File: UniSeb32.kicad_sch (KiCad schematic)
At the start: 35 parts

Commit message: -
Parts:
- removed X7: (no value), symbol UniSeb8266-eagle-import:0446200002
- added C?: 100n, symbol Device:C_Small
- added J2: ARJM11C7-114-BA-EW2, Connector_RJ:RJ45_Abracon_ARJM11C-BA, symbol Connector-custom:RJ45_Abracon_ARJM11C7-114
- added R? (x2): 2.2k, Resistor_SMD:R_0603_1608Metric, symbol Device:R
- added R? (x4): 49.9 %1, Resistor_SMD:R_0603_1608Metric, symbol Device:R
- added R?: 0, Resistor_SMD:R_0603_1608Metric, symbol Device:R
- C1: value (none) -> 100µF; footprint (none) -> UniSeb8266:E2,5-6
- C2: value (none) -> 22µF; footprint (none) -> UniSeb8266:E2,5-6
- F1: value (none) -> 200mA MT; footprint (none) -> UniSeb8266:TR5
- F2: value (none) -> 1A T; footprint (none) -> UniSeb8266:TR5
- I2C-1, I2C-2, I2C-3: value (none) -> MA05-1_WON; footprint (none) -> UniSeb8266:MA05-1_WON
- IC1: value (none) -> WEMOS-D1-MINI; footprint (none) -> UniSeb8266:WEMOS-D1-MINI
- IC2: value (none) -> GY-BME280-3.3; footprint (none) -> UniSeb8266:GY-BME280-3.3
- IC3: value (none) -> AMS1117-3.3; footprint (none) -> UniSeb8266:SOT223
- IC4: value (none) -> MCP23008SS; footprint (none) -> UniSeb8266:SSOP20
- IC5: value (none) -> RT9400; footprint (none) -> UniSeb8266:RT9400
- IC6: value (none) -> AMS5915; footprint (none) -> UniSeb8266:AMS5915
- J1: value (none) -> 22-?-0327-2031; footprint (none) -> UniSeb8266:6410-03
- LED1: value (none) -> LED3MM; footprint (none) -> UniSeb8266:LED3MM
- R1: value (none) -> 33/1W; footprint (none) -> UniSeb8266:P0613V
- R2: renamed from R?; footprint (none) -> Resistor_SMD:R_0603_1608Metric
- R3: value (none) -> 390; footprint (none) -> UniSeb8266:R1206
- R4: value (none) -> 10k; footprint (none) -> UniSeb8266:R1206
- R5: value (none) -> 4,7k; footprint (none) -> UniSeb8266:R1206
- R6, R7: value (none) -> R-EU_R1206; footprint (none) -> UniSeb8266:R1206
- SJ1: value (none) -> SJ; footprint (none) -> UniSeb8266:SJ
- SJ2: value (none) -> SJ2W; footprint (none) -> UniSeb8266:SJ_2
- U$2: value (none) -> HLK-PM01; footprint (none) -> UniSeb8266:HLK-PM01
- X1, X2: value (none) -> AK500/2; footprint (none) -> UniSeb8266:AK500_2
- X3: value (none) -> 233-503; footprint (none) -> UniSeb8266:233-503
- X5: value (none) -> 233-504; footprint (none) -> UniSeb8266:233-504
- X61: value (none) -> JST-XH-05-PIN-LONG-PAD; footprint (none) -> UniSeb8266:JST-XH-05-PACKAGE-LONG-PAD
- X8: value (none) -> 233-508; footprint (none) -> UniSeb8266:233-508
- gave numbers to parts that had none: 3
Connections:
- net 3V3: now also J2.11 (RLED+), R?.1, R?.1, R?.1, R?.1, R?.2
- net GND: now also C?.1, R?.2, R?.2
- net at U2.20 (TXN): now also J2.8 (TD-), R?.2
- net at U2.21 (TXP): now also J2.10 (TD+), R?.2
- net at U2.22 (RXN): now also J2.3 (RD-), R?.2
- net at U2.23 (RXP): now also J2.5 (RD+), R?.2
- net at U2.3 (LED1/REGOFF): now also J2.13 (LLED+)
- net VA2: now reaches IC5.P$2 (VA2)
- net VA2: now also J2.2 (VC1-)
- net VA1: now reaches IC5.P$1 (VA1)
- net VA1: now also J2.7 (VC1+)
- net VB1: now reaches IC5.P$3 (VB1)
- net VB1: now also J2.6 (VC2+)
- net VB2: now reaches IC5.P$4 (VB2)
- net VB2: now also J2.1 (VC2-)
- new net: J2.12 (RLED-), R?.1
- new net: J2.14 (LLED-), R?.1
- new net: C?.2, J2.4 (RCT), J2.9 (TCT), R?.1
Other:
- moved on the sheet: C3, R2, U1, U2

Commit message: .
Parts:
- added C? (x2): 100n, symbol Device:C_Small
- added C? (x4): 10p, symbol Device:C_Small
- added C?: 10uf, symbol Device:C_Small
- added C?: 22µ, symbol Device:C_Small
- added C?: 2.2µ, symbol Device:C_Small
- added C?: 10n, symbol Device:C_Small
- added L?: L, Inductor_SMD:L_0805_2012Metric, symbol Device:L
- added R?: 12.1k, Resistor_SMD:R_0603_1608Metric, symbol Device:R
- C?: jlcpcb (none) -> C14663
- R? (x2): jlcpcb (none) -> C22938
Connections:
- net 3V3: now also U2.9 (VDDIO), C?.1, C?.1, L?.1; no longer R?.1, R?.1, R?.1, R?.1, R?.2
- net GND: now also U2.25 (VSS), C?.2, C?.2, C?.2, C?.2, C?.2, C?.2, C?.2, C?.2, C?.2, C?.2, R?.2
- net 3V3-2: now reaches U2.1 (VDD2A)
- net 3V3-2: now also R?.1, R?.1, R?.1, R?.1, R?.2, U2.19 (VDD1A), C?.1, C?.1, L?.2
- net at J2.8 (TD-), R?.2, U2.20 (TXN): now also C?.1
- net at J2.10 (TD+), R?.2, U2.21 (TXP): now also C?.1
- net at J2.3 (RD-), R?.2, U2.22 (RXN): now also C?.1
- net at J2.5 (RD+), R?.2, U2.23 (RXP): now also C?.1
- net at U2.24 (RBIAS): now also R?.1
- net at U2.6 (VDDCR): now also C?.1, C?.1

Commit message: .
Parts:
- added C? (x2): 30p, symbol Device:C_Small
- added R? (x6): 10k, Resistor_SMD:R_0603_1608Metric, symbol Device:R
- added Y?: Crystal_GND23, Crystal:Crystal_SMD_3225-4Pin_3.2x2.5mm, symbol Device:Crystal_GND23
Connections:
- net 3V3-2: now also R?.2, R?.2, R?.2, R?.2, R?.2
- net GND: now also C?.2, C?.2, R?.1, Y?.2, Y?.3
- net at U2.10 (RXER/PHYAD0): now also R?.2
- net EMAC_CRS_DV: now reaches U2.11 (CRS_DV/MODE2)
- net EMAC_CRS_DV: now also U1.12 (IO27), R?.1
- net EMAC_MDIO: now reaches U2.12 (MDIO)
- net EMAC_MDIO: now also U1.30 (IO18), R?.1
- net EMAC_MDC: now reaches U2.13 (MDC)
- net EMAC_MDC: now also U1.37 (IO23)
- net IO5_RST: now reaches U2.15 (RST)
- net IO5_RST: now also U1.29 (IO5), R?.1
- net EMAC_TX_EN: now reaches U2.16 (TXEN)
- net EMAC_TX_EN: now also U1.33 (IO21)
- net EMAC_TXD0: now reaches U2.17 (TXD0)
- net EMAC_TXD0: now also U1.31 (IO19)
- net EMAC_TXD1: now reaches U2.18 (TXD1)
- net EMAC_TXD1: now also U1.36 (IO22)
- net at U2.4 (XTAL2): now also C?.1, Y?.4
- net at U2.5 (XTAL1/CLKIN): now also C?.1, Y?.1
- net EMAC_RXD1: now reaches U2.7 (RXD1/MODE1)
- net EMAC_RXD1: now also U1.11 (IO26), R?.1
- net EMAC_RXD0: now reaches U2.8 (RXD0/MODE0)
- net EMAC_RXD0: now also U1.10 (IO25), R?.1
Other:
- moved on the sheet: R?

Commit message: .
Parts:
- added C? (x2): 22µ, symbol Device:C_Small
- added U?: BOT, Switches-Custom:Tactile Push Button 3X6X2.5mm, symbol Switches-Custom:SMD-Switch
- added U?: RST, Switches-Custom:Tactile Push Button 3X6X2.5mm, symbol Switches-Custom:SMD-Switch
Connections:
- net 3V3: now also C?.1, C?.2
- net GND: now also J2.15 (SHIELD), C?.1, C?.2, U?.2 (B), U?.2 (B)
- net IO17_RCLK: now reaches C?.1, U2.5 (XTAL1/CLKIN), Y?.1
- net IO17_RCLK: now also U1.28 (IO17)
- net at C3.2, R2.2: now also U?.1 (A); no longer U1.3 (EN)
- net IO0: now reaches U1.25 (IO0)
- net IO0: now also U?.1 (A)
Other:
- moved on the sheet: C3, C?, R2, Y?

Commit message: .
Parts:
- removed C3: 4.7u, symbol Device:C
- removed C? (x2): 22µ, symbol Device:C_Small
- removed IC1: WEMOS-D1-MINI, UniSeb8266:WEMOS-D1-MINI, symbol UniSeb8266-eagle-import:WEMOS-D1-MINI
- removed R2: 100k, Resistor_SMD:R_0603_1608Metric, symbol Device:R
- removed SJ1: SJ, UniSeb8266:SJ, symbol UniSeb8266-eagle-import:SJ
- removed SJ2: SJ2W, UniSeb8266:SJ_2, symbol UniSeb8266-eagle-import:SJ2W
- removed U1: ESP32-WROOM-32, RF_Module:ESP32-WROOM-32, symbol RF_Module:ESP32-WROOM-32
- removed U?: BOT, Switches-Custom:Tactile Push Button 3X6X2.5mm, symbol Switches-Custom:SMD-Switch
- removed U?: RST, Switches-Custom:Tactile Push Button 3X6X2.5mm, symbol Switches-Custom:SMD-Switch
- added JP1: SolderJumper_2_Open, symbol Jumper:SolderJumper_2_Open
- added JP2: SolderJumper_3_Open, Jumper:SolderJumper-3_P1.3mm_Open_Pad1.0x1.5mm_NumberLabels, symbol Jumper:SolderJumper_3_Open
- added U1: mini_esp32, ESP32_mini:ESP32_mini, symbol ESP32_mini:mini_esp32
- gave numbers to parts that had none: 29
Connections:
- net 3V3 is gone; now on net +3.3V: C13.1, C3.1, J2.11 (RLED+), L1.1, U2.9 (VDDIO)
- net +5V: now also JP1.1 (A), U1.35 (VCC_(USB))
- net COUNTER: now also U1.11 (IO_34)
- net EMAC_CRS_DV: now also U1.24 (IO_27)
- net EMAC_MDC: now also U1.12 (IO_23/D7)
- net EMAC_MDIO: now also U1.8 (IO_18/D5)
- net EMAC_RXD0: now also U1.26 (IO_25)
- net EMAC_RXD1: now also U1.6 (IO_26/D0)
- net EMAC_TXD1: now also U1.25 (IO_22/D1/SCL)
- net EMAC_TX_EN: now also U1.27 (IO_21/D2/SDA)
- net GND: now also U1.1 (GND), U1.22 (GND), U1.33 (GND)
- net IO0: now also U1.34 (IO_00)
- net IO17_RCLK: now also U1.29 (IO_17/D3)
- net IO5_RST: now also U1.14 (IO_05/D8)
- net ONEWIRE: now also U1.18 (IO_13/TCK)
- net SCL: now also U1.32 (IO_04)
- net SDA: now also U1.36 (IO_02)
- net SDS_RX: now also U1.13 (IO_14/TMS)
- net SDS_TX: now also U1.30 (IO_12/TDI)
- net VCC: now also JP1.2 (B)
- net at IC5.P$6 (+VDC), R7.1, U$2.+5V: now also JP2.1 (A)
- net at F2.1: now also JP2.2 (C)
- net at X2.1 (KL): now also JP2.3 (B)
- net +3V3 renamed +3.3V
- net D0 renamed IO32
- net IO32: now also U1.28 (IO_32)
- net D5 renamed IO33
- net IO33: now also U1.9 (IO_33)
- net EXP-INT: no longer names the net of IC4.8 (INT)
- new net EMAC_TXDO: U1.10 (IO_19/D6)
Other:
- moved on the sheet: C1, C3, L1, LED1, R16, R17, R18, R19, R20, R3

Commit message: .
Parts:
- removed C1: 100µF, UniSeb8266:E2,5-6, symbol UniSeb8266-eagle-import:CPOL-EUE2.5-6
- removed C2: 22µF, UniSeb8266:E2,5-6, symbol UniSeb8266-eagle-import:CPOL-EUE2.5-6
- removed F1: 200mA MT, UniSeb8266:TR5, symbol UniSeb8266-eagle-import:TR5
- removed F2: 1A T, UniSeb8266:TR5, symbol UniSeb8266-eagle-import:TR5
- removed I2C-1, I2C-2, I2C-3: MA05-1_WON, UniSeb8266:MA05-1_WON, symbol UniSeb8266-eagle-import:MA05-1_WON
- removed IC2: GY-BME280-3.3, UniSeb8266:GY-BME280-3.3, symbol UniSeb8266-eagle-import:GY-BME280-3.3
- removed IC3: AMS1117-3.3, UniSeb8266:SOT223, symbol UniSeb8266-eagle-import:LM1117IMPX-
- removed IC4: MCP23008SS, UniSeb8266:SSOP20, symbol UniSeb8266-eagle-import:MCP23008SS
- removed IC5: RT9400, UniSeb8266:RT9400, symbol UniSeb8266-eagle-import:RT9400
- removed IC6: AMS5915, UniSeb8266:AMS5915, symbol UniSeb8266-eagle-import:AMS5915
- removed J1: 22-?-0327-2031, UniSeb8266:6410-03, symbol UniSeb8266-eagle-import:22-?-0327-2031
- removed J2: ARJM11C7-114-BA-EW2, Connector_RJ:RJ45_Abracon_ARJM11C-BA, symbol Connector-custom:RJ45_Abracon_ARJM11C7-114
- removed LED1: LED3MM, UniSeb8266:LED3MM, symbol UniSeb8266-eagle-import:LED3MM
- removed R1: 33/1W, UniSeb8266:P0613V, symbol UniSeb8266-eagle-import:R-EU_0613/5V
- removed R3: 390, UniSeb8266:R1206, symbol UniSeb8266-eagle-import:R-EU_R1206
- removed R4: 10k, UniSeb8266:R1206, symbol UniSeb8266-eagle-import:R-EU_R1206
- removed R5: 4,7k, UniSeb8266:R1206, symbol UniSeb8266-eagle-import:R-EU_R1206
- removed R6, R7: R-EU_R1206, UniSeb8266:R1206, symbol UniSeb8266-eagle-import:R-EU_R1206
- removed U$2: HLK-PM01, UniSeb8266:HLK-PM01, symbol UniSeb8266-eagle-import:HLK-PM01
- removed X1, X2: AK500/2, UniSeb8266:AK500_2, symbol UniSeb8266-eagle-import:AK500/2
- removed X3: 233-503, UniSeb8266:233-503, symbol UniSeb8266-eagle-import:233-503
- removed X5: 233-504, UniSeb8266:233-504, symbol UniSeb8266-eagle-import:233-504
- removed X61: JST-XH-05-PIN-LONG-PAD, UniSeb8266:JST-XH-05-PACKAGE-LONG-PAD, symbol UniSeb8266-eagle-import:JST-XH-05-PIN-LONG-PAD
- removed X8: 233-508, UniSeb8266:233-508, symbol UniSeb8266-eagle-import:233-508
- added C1: 100µ, Capacitor_THT:CP_Radial_D5.0mm_P2.50mm, symbol Device:C_Polarized_Small
- added C2: 22µ tantalium, Capacitor_THT:CP_Radial_D5.0mm_P2.50mm, symbol Device:C_Polarized_Small
- added F1: 200mA MT, Fuse:Fuse_Littelfuse_372_D8.50mm, symbol Device:Fuse
- added F2: 550mA MT, Fuse:Fuse_Littelfuse_372_D8.50mm, symbol Device:Fuse
- added J1: IO, Connector:FanPinHeader_1x03_P2.54mm_Vertical, symbol Connector_Generic:Conn_01x03
- added J2: ARJM11C7-114-BA-EW2, _custom:ARJM11C7-114-BA-EW2, symbol _custom:ARJM11C7-114-BA-EW2
- added J3: Conn_02x05_Odd_Even, Connector_PinHeader_2.54mm:PinHeader_2x05_P2.54mm_Vertical_SMD, symbol Connector_Generic:Conn_02x05_Odd_Even
- added J6: SDS011, Connector_JST:JST_XH_B5B-XH-A_1x05_P2.50mm_Vertical, symbol Connector_Generic:Conn_01x05
- added J7, J8: Conn_01x02_Female, TerminalBlock:TerminalBlock_bornier-2_P5.08mm, symbol Connector:Conn_01x02_Female
- added R1: 33/1W, Resistor_THT:R_Axial_DIN0414_L11.9mm_D4.5mm_P5.08mm_Vertical, symbol Device:R
- added R4: 10k, Resistor_SMD:R_0603_1608Metric, symbol Device:R
- added R5: 4,7k, Resistor_SMD:R_0603_1608Metric, symbol Device:R
- added R6, R7: R, Resistor_SMD:R_0603_1608Metric, symbol Device:R
- added U3: AMS1117-3.3, Package_TO_SOT_SMD:SOT-223-3_TabPin2, symbol Regulator_Linear:AMS1117-3.3
- added U4: AMS5919, _custom:AMS5915, symbol _custom:AMS5919
- added U5: module_bme280, usini_sensors:module_bme280, symbol usini_sensors:module_bme280
- added U6: RT9400, _custom:RT9400, symbol _custom:RT9400
- added U7: MCP23008-xSS, Package_SO:SSOP-20_5.3x7.2mm_P0.65mm, symbol Interface_Expansion:MCP23008-xSS
- added U8: HLK-PM01, Converter_ACDC:Converter_ACDC_HiLink_HLK-PMxx, symbol Converter_ACDC:HLK-PM01
- added X1: 233-508, con-wago:con-wago-233-508, symbol con-wago:233-508
- added X2: 233-503, con-wago:con-wago-233-503, symbol con-wago:233-503
- added X3: 233-504, con-wago:con-wago-233-504, symbol con-wago:233-504
- C10, C11, C12, C13, C14, C15, C4, C5, C6, C7, C8, C9: footprint (none) -> Capacitor_SMD:C_0603_1608Metric
- C3: footprint (none) -> Capacitor_SMD:C_1206_3216Metric
- JP1: footprint (none) -> Jumper:SolderJumper-2_P1.3mm_Open_Pad1.0x1.5mm
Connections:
- net +3.3V: now also C2.1, J2.11 (RLED+), J3.1 (Pin_1), J3.2 (Pin_2), R4.2, R5.2, U3.2 (VO), U4.2 (VCC), U5.1 (VCC), U7.20 (VDD), U7.6 (~{RESET}), X2.B3 (B-3)
- net +5V: now also C1.1, J3.3 (Pin_3), J3.4 (Pin_4), J6.4 (Pin_4), U3.3 (VI), X2.B1 (B-1), X3.B3 (B-3)
- net COUNTER: now also R4.1, X3.B2 (B-2)
- net GND: now also C7.1, C1.2, C2.2, J1.1 (Pin_1), J2.SH (SHIELD), J3.5 (Pin_5), J3.6 (Pin_6), J6.3 (Pin_3), J8.1 (Pin_1), R1.1, R6.1, U3.1 (GND), U4.1 (GND), U5.2 (GND), U6.P$5 (-VDC), U7.3 (A2), U7.4 (A1), U7.5 (A0), U7.9 (VSS), U8.3 (-Vout), X2.B2 (B-2), X3.B4 (B-4); no longer C7.2
- net IO17_RCLK: now also Y1.4; no longer Y1.1
- net IO32: now also J1.3 (Pin_3)
- net IO33: now also J1.2 (Pin_2)
- net ONEWIRE: now also R5.1, X3.B1 (B-1)
- net SCL: now also J3.7 (Pin_7), J3.8 (Pin_8), U4.4 (SCL), U5.3 (SCL), U7.1 (SCL)
- net SDA: now also J3.10 (Pin_10), J3.9 (Pin_9), U4.3 (SDA), U5.4 (SDA), U7.2 (SDA)
- net SDS_RX: now also J6.2 (Pin_2)
- net SDS_TX: now also J6.1 (Pin_1)
- net VA1: now also J2.7 (VC1+), U6.P$1 (VA1)
- net VA2: now also J2.2 (VC1-), U6.P$2 (VA2)
- net VB1: now also J2.6 (VC2+), U6.P$3 (VB1)
- net VB2: now also J2.1 (VC2-), U6.P$4 (VB2)
- net VCC: now also F2.2, R1.2
- net at R11.2, U2.23 (RXP): now also C7.2, J2.5 (RD+); no longer C7.1
- net at R12.1: now also J2.12 (RLED-)
- net at C6.1, R10.2, U2.20 (TXN): now also J2.8 (TD-)
- net at C5.1, R9.2, U2.21 (TXP): now also J2.10 (TD+)
- net at C8.1, R13.2, U2.22 (RXN): now also J2.3 (RD-)
- net at U2.3 (LED1/REGOFF): now also J2.13 (LLED+)
- net at C14.1, U2.4 (XTAL2): now also Y1.1; no longer Y1.4
- net at JP2.1 (A): now also R7.2, U6.P$6 (+VDC), U8.4 (+Vout)
- net at JP2.2 (C): now also F2.1
- net at JP2.3 (B): now also J8.2 (Pin_2)
- net at R8.1: now also J2.14 (LLED-)
- net at C4.2, R2.1: now also J2.4 (RCT), J2.9 (TCT)
- new net: F1.1, J7.1 (Pin_1)
- new net: J7.2 (Pin_2), U8.1 (AC/L)
- new net: R6.2, R7.1, U6.P$7 (ADJ)
- new net: F1.2, U8.2 (AC/N)
- new net: U7.12 (GP0), X1.B1 (B-1)
- new net: U7.13 (GP1), X1.B2 (B-2)
- new net: U7.14 (GP2), X1.B3 (B-3)
- new net: U7.15 (GP3), X1.B4 (B-4)
- new net: U7.16 (GP4), X1.B5 (B-5)
- new net: U7.17 (GP5), X1.B6 (B-6)
- new net: U7.18 (GP6), X1.B7 (B-7)
- new net: U7.19 (GP7), X1.B8 (B-8)
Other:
- note added: "ext. 5V powersupply"
- note removed: "5V-Netzteil"
- note removed: "tantalum"
- moved on the sheet: C7

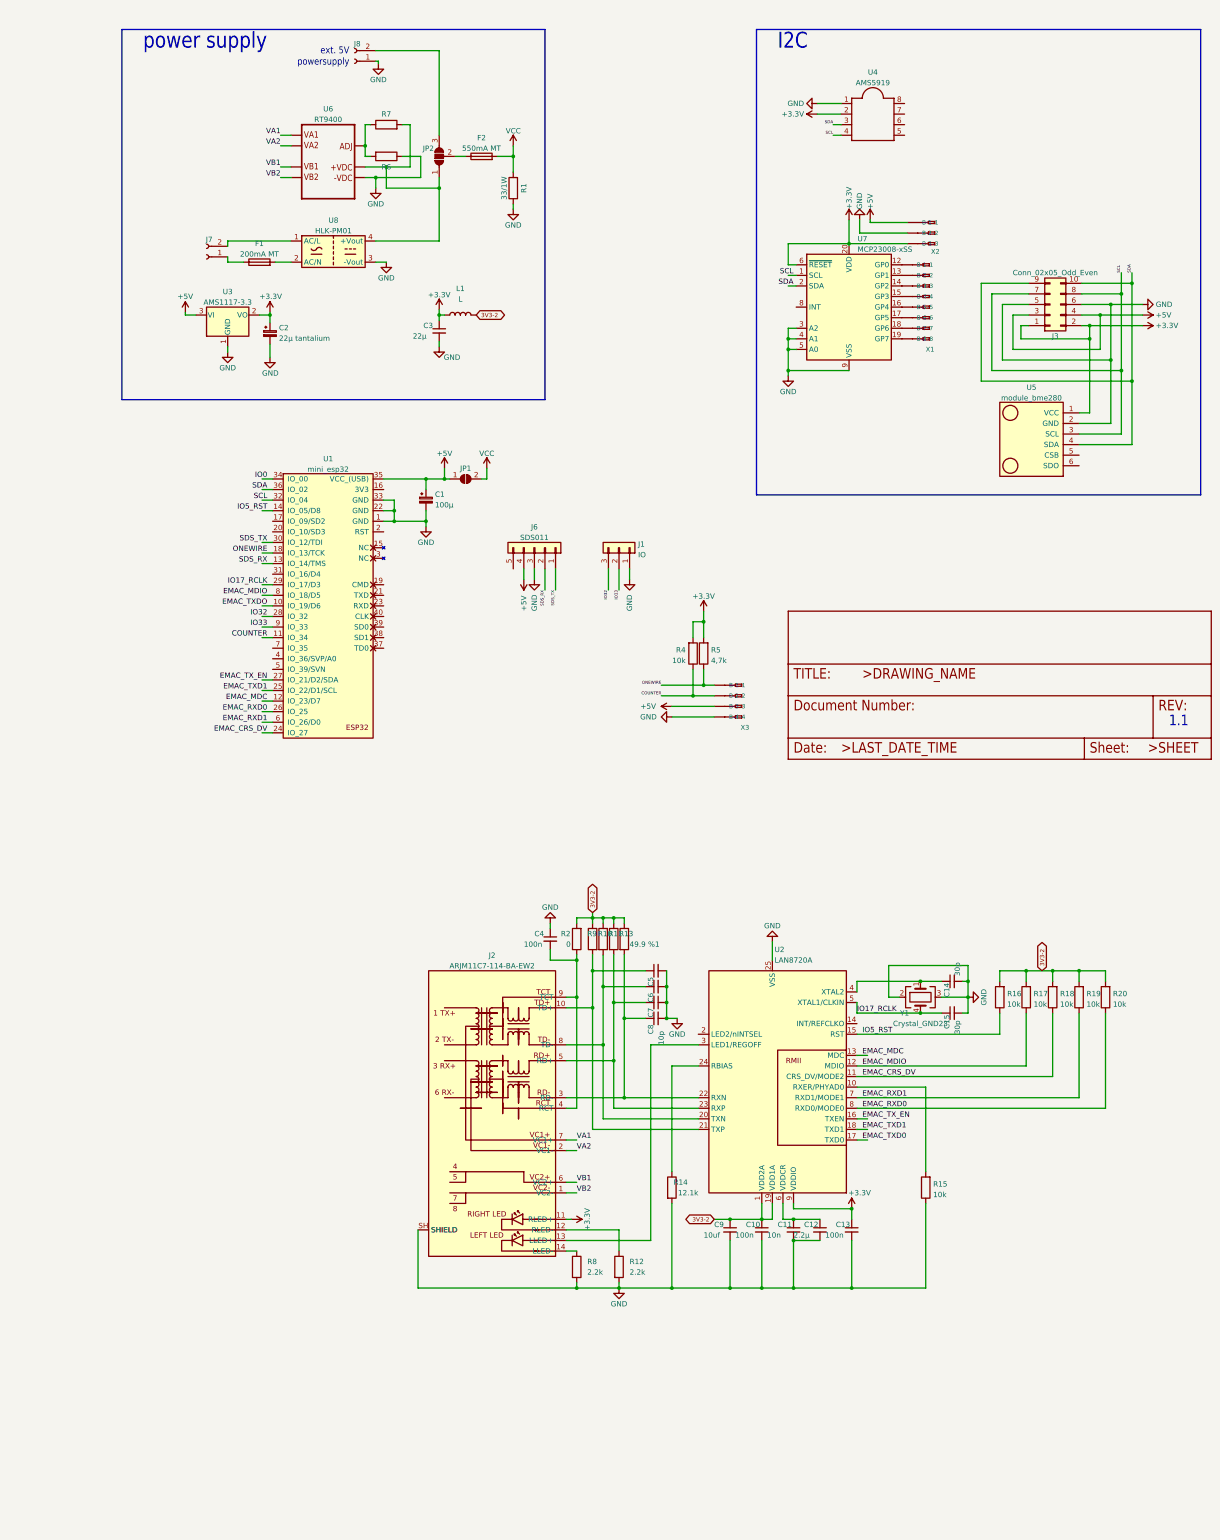
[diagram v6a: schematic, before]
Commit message: switched to 4 layer PCB. Routed remaining airwires
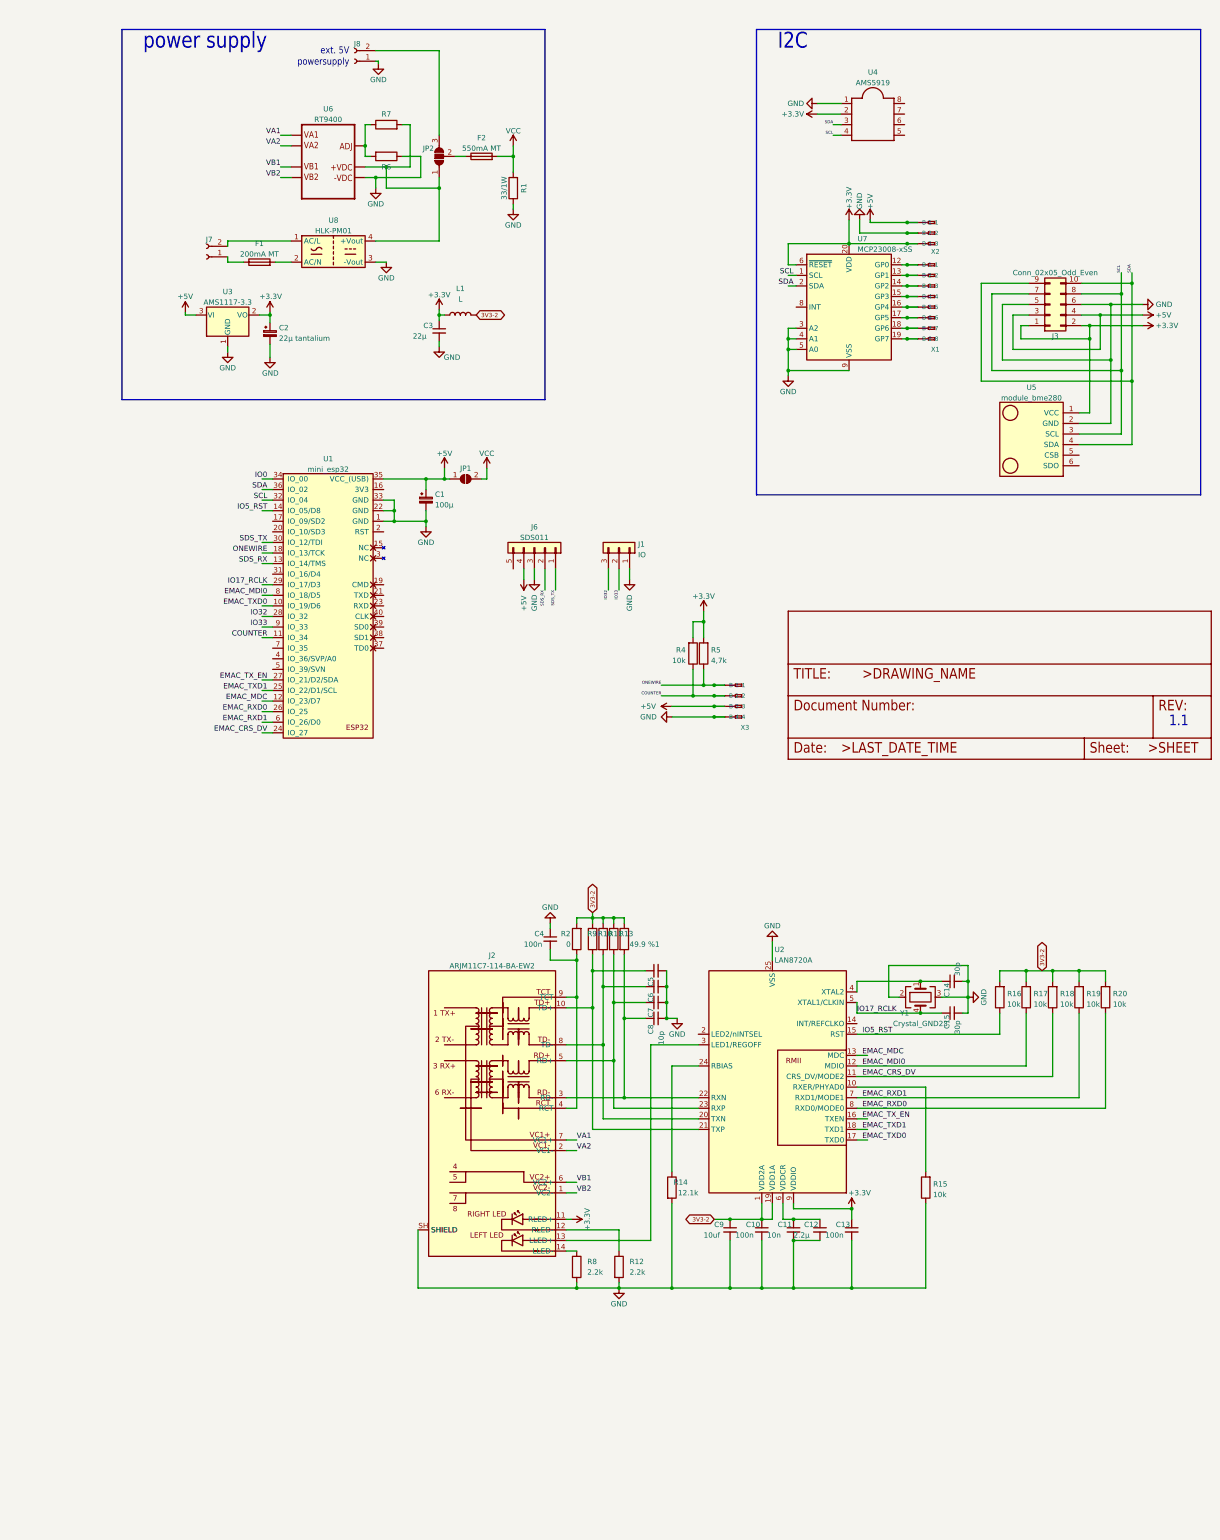
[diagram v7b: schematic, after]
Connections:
- net EMAC_TXDO is gone; now on net EMAC_TXD0: U1.10 (IO_19/D6)
- net +3.3V: now also X2.A3 (-3)
- net +5V: now also X2.A1 (-1), X3.A3 (-3)
- net COUNTER: now also X3.A2 (-2)
- net GND: now also X2.A2 (-2), X3.A4 (-4)
- net ONEWIRE: now also X3.A1 (-1)
- net at X1.A1 (-1): now also U7.12 (GP0), X1.B1 (B-1)
- net at X1.A2 (-2): now also U7.13 (GP1), X1.B2 (B-2)
- net at X1.A3 (-3): now also U7.14 (GP2), X1.B3 (B-3)
- net at X1.A4 (-4): now also U7.15 (GP3), X1.B4 (B-4)
- net at X1.A5 (-5): now also U7.16 (GP4), X1.B5 (B-5)
- net at X1.A6 (-6): now also U7.17 (GP5), X1.B6 (B-6)
- net at X1.A7 (-7): now also U7.18 (GP6), X1.B7 (B-7)
- net at X1.A8 (-8): now also U7.19 (GP7), X1.B8 (B-8)
- net EMAC_MDIO renamed EMAC_MDI0
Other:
- moved on the sheet: X1
